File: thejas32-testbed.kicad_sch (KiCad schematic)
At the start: 101 parts, among them J1 Conn_01x04, J10 Conn_02x10_Odd_Even, J11 Conn_01x03, J12 Conn_02x20_Odd_Even, J13 Conn_01x03, J2 USB_B_Micro, J3 Conn_02x03_Odd_Even, J4 Conn_02x05_Odd_Even, J6 Conn_01x10, J7 Conn_01x05, J8 Conn_01x03, J9 Conn_01x05, U1 Pico Master, U2 THEJAS32, U6 W25Q16JVSSIQ

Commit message: Incorporated most review comments.
Used 5 mils traces in breakout area. This results in very few DRC
errors iff track spacing is set to 5 mils.  However, setting it to
8 mils (in board settings) does complain essentially for every pad
of the THEJAS32. Those just need to be waived off.

Ensure 16 mils track separation, except in breakout area. This can
be verified by setting the track spacing to 16 mils and running the
DRC. Except for the core area, and some issues on the USB connector,
no other errors must pop up.

Poured copper on every layer. Added GND vias to increase GND pour.

Moved flash IC to improve routing to the GPIO connector.

Moved USB connector close to the RP2040s USB connector, J3 placed
next to it. So both jumpers are now close.

Added MPN field, and populated it for many components, except caps
and headers.

Pending: Power nets are routed at 12 mils from THEJAS32. Get it down
to 5 mil ?
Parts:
- removed H5: MountingHole, MountingHole:MountingHole_3mm, symbol Mechanical:MountingHole
- R1, R16, R18, R20, R22, R24, R25, R26, R28, R29, R30, R31, R32, R33, R34, R35, R36, R37, R70: value 0E -> 27E; MPN (none) -> 27E
- R2, R38, R39, R40, R41, R42, R43: MPN (none) -> 10K
- R4, R5, R6, R7, R8, R9: MPN (none) -> 2.2K
- TP1: footprint MountingHole:MountingHole_3mm_Pad_TopBottom -> MountingHole:MountingHole_3.2mm_M3_Pad_TopBottom
- U1: MPN (none) -> Raspberry Pi Pico
- U2: MPN (none) -> THEJAS32
- U4, U5: MPN (none) -> Mini360
- U6: MPN (none) -> W25Q16JVSSIQ
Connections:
- net GND: now also J10.1 (Pin_1), J10.2 (Pin_2); no longer J10.19 (Pin_19), J10.20 (Pin_20)
- net PWR_3V3: now also J10.19 (Pin_19), J10.20 (Pin_20); no longer J10.1 (Pin_1), J10.2 (Pin_2)
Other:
- note added: "Jumper Meaning ------------------------------------------------------------- JP3 JP4 | ------------------------------------------------------------- Y Y | 5V from USB connector is used for the entire board. | Pico must not get power from host. | Pico can be used as USB host. ------------------------------------------------------------- N Y | 5V from USB connector is used for Thejas32 only. | Pico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"
- note added: "Power for THEJAS32"
- note added: "THEJAS32 Core Circuit"
- moved on the sheet: C1, C10, C10A1, C11, C11A1, C12, C12A1, C13, C14, C15, C16, C17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

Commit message: Cleanup and beautification for review.
Added silkscreen for all components.
Grouped schematic for reading clarity.
No circuit level changes, few nets renamed.
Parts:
- R1, R70: value 27E -> 10E; MPN 27E -> 10E
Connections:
- net MCU_BOOT_UART_RX: now also J3.3 (Pin_3), U2.107 (UART0_RX); no longer J3.4 (Pin_4), U1.6 (GPIO4)
- net MCU_BOOT_UART_TX: now also J3.1 (Pin_1), U2.108 (UART0_TX); no longer J3.2 (Pin_2), U1.7 (GPIO5)
- net MCU_UART1_TX: now reaches J11.1 (Pin_1), U2.45 (UART1_TX)
- net MCU_UART1_RX: now reaches J11.2 (Pin_2), U2.50 (UART1_RX)
- new net MCU_BOOT_UART_RX_PICO: J3.4 (Pin_4), U1.6 (GPIO4)
- new net MCU_BOOT_UART_TX_PICO: J3.2 (Pin_2), U1.7 (GPIO5)
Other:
- note added: "10K to ground, following official docs"
- note added: "Boot UART Tapping Header"
- note added: "GPOUT clock serves as the clock for THEJAS32. Nominal clock 100 MHz"
- note added: "Headers to tap I2C and SPI comms between THEJAS32 and Pico"
- note added: "JTAG connections"
- note added: "Jumper Usage"
- note added: "Pull-ups used as THEJAS32 doesn't have internal ones. Depop if not required."
- note added: "Raspberry Pi HAT Compatibility"
- note added: "Test Driver (Raspberry Pico)"
- note added: "This header is to help plug common hats and get them to work. From a pinmux and functionality perspective, thejas32 doesn't match the RPi, but this provides useful compatibility for commonly used pins. Thejas pins don't have pinmuxing. E.g. UART pins can't be used as GPIOs... The following are ensured: 3.3V, 5V for appropriately powering the HATs I2C on pins 3,5 UART RX, TX on pins 8, 10 SPI with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"
- note added: "User Headers"
- note removed: "GPOUT clock serves as the clock for THEJAS32"
- note removed: "Raspberry Pi Compatibility Header This header is to help plug common hats and get them to work. From a pinmux and functionality perspective, thejas32 doesn't match the RPi so it's a no-brainer that you should expect only some useful compatibility. Bear in mind that thejas pins have single functionality. E.g. UART pins can't be used as GPIOs... The following are ensured: 3.3V, 5V for appropriately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"
- moved on the sheet: H1, H2, H3, H4, J1, J10, J12, J13, J2, J3, J4, J6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

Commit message: Ready for review, all comments included
All MPNs are provided
Silkscreen updated
BOM generation corrected.
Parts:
- C1, C10, C11, C12, C13, C14, C15, C16, C17, C18, C19, C2, C20, C21, C22, C23, C24, C25, C3, C4, C5, C6, C7, C8, C9: MPN (none) -> 100nF
- C10A1, C11A1, C12A1, C1A1, C25A1, C2A1, C3A1, C4A1, C5A1, C6A1, C7A1, C8A1, C9A1: MPN (none) -> 10uF
- H1, H2, H3, H4, TP1, TP2, TP4, TP6, TP7: now left out of the parts list
- J1: MPN (none) -> 2.54 mm 1x4 pin male header
- J10: MPN (none) -> 2.54 mm 2x10 pin male header
- J11, J13, J8: MPN (none) -> 2.54 mm 1x3 pin male header
- J12: MPN (none) -> 2.54 mm 2x20 pin male header
- J3: MPN (none) -> 2.54 mm 2x3 pin male header
- J4: MPN (none) -> 2.54 mm 2x5 pin male header
- J6: MPN (none) -> 2.54 mm 1x10 pin male header
- J7, J9: MPN (none) -> 2.54 mm 1x5 pin male header
- JP1, JP2, JP3, JP4: MPN (none) -> 2.54 mm 1x2 pin male header
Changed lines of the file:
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@@
 			)
 		)
-		(property "MPN" ""
+		(property "MPN" "100nF"
 			(at 27.94 162.56 0)
 			(effects
@@
 			)
 		)
-		(property "MPN" ""
+		(property "MPN" "2.54 mm 1x5 pin male header"
 			(at 472.44 492.76 0)
 			(effects
@@
 			)
 		)
-		(property "MPN" ""
+		(property "MPN" "100nF"
 			(at 54.61 219.71 0)
 			(effects
@@
 			)
 		)
-		(property "MPN" ""
+		(property "MPN" "2.54 mm 1x10 pin male header"
 			(at 542.29 335.28 0)
 			(effects
@@
 			)
 		)
-		(property "MPN" ""
+		(property "MPN" "100nF"
 			(at 81.28 290.83 0)
 			(effects
@@
 			)
 		)
-		(property "MPN" ""
+		(property "MPN" "2.54 mm 1x3 pin male header"
 			(at 275.59 316.23 0)
 			(effects
@@
 			)
 		)
-		(property "MPN" ""
+		(property "MPN" "10uF"
 			(at 39.37 167.64 0)
 			(effects
@@
 			)
 		)
-		(property "MPN" ""
+		(property "MPN" "2.54 mm 1x5 pin male header"
 			(at 294.64 551.18 0)
 			(effects
@@
 			)
 		)
-		(property "MPN" ""
+		(property "MPN" "100nF"
 			(at 101.6 243.84 0)
 			(effects
@@
 			)
 		)
-		(property "MPN" ""
+		(property "MPN" "100nF"
 			(at 92.71 243.84 0)
 			(effects
@@
 		(unit 1)
 		(exclude_from_sim no)
-		(in_bom yes)
+		(in_bom no)
 		(on_board yes)
 		(dnp no)
@@
 			)
 		)
-		(property "MPN" ""
+		(property "MPN" "100nF"
 			(at 92.71 265.43 0)
 			(effects
@@
 			)
 		)
-		(property "MPN" ""
+		(property "MPN" "100nF"
 			(at 82.55 243.84 0)
 			(effects
@@
 			)
 		)
-		(property "MPN" ""
+		(property "MPN" "100nF"
 			(at 80.01 123.19 0)
 			(effects
@@
 			)
 		)
-		(property "MPN" ""
+		(property "MPN" "100nF"
 			(at 100.33 290.83 0)
 			(effects
@@
 		(unit 1)
 		(exclude_from_sim no)
-		(in_bom yes)
+		(in_bom no)
 		(on_board yes)
 		(dnp no)
@@
 			)
 		)
-		(property "MPN" ""
+		(property "MPN" "100nF"
 			(at 101.6 265.43 0)
 			(effects
@@
 			)
 		)
-		(property "MPN" ""
+		(property "MPN" "100nF"
 			(at 93.98 219.71 0)
 			(effects
@@
 			)
 		)
-		(property "MPN" ""
+		(property "MPN" "100nF"
 			(at 370.84 295.91 0)
 			(effects
@@
 			)
 		)
-		(property "MPN" ""
+		(property "MPN" "2.54 mm 1x2 pin male header"
 			(at 576.58 213.36 0)
 			(effects
@@
 		(unit 1)
 		(exclude_from_sim no)
-		(in_bom yes)
+		(in_bom no)
 		(on_board yes)
 		(dnp no)
@@
 			)
 		)
-		(property "MPN" ""
+		(property "MPN" "2.54 mm 2x5 pin male header"
 			(at 378.46 547.37 0)
 			(effects
@@
 			)
 		)
-		(property "MPN" ""
+		(property "MPN" "2.54 mm 1x4 pin male header"
 			(at 643.89 313.69 0)
 			(effects
@@
 			)
 		)
-		(property "MPN" ""
+		(property "MPN" "100nF"
 			(at 327.66 132.08 0)
 			(effects
@@
 		(unit 1)
 		(exclude_from_sim no)
-		(in_bom yes)
+		(in_bom no)
 		(on_board yes)
 		(dnp no)
@@
 			)
 		)
-		(property "MPN" ""
+		(property "MPN" "2.54 mm 1x3 pin male header"
 			(at 566.42 303.53 0)
 			(effects
@@
 			)
 		)
-		(property "MPN" ""
+		(property "MPN" "100nF"
 			(at 82.55 265.43 0)
 			(effects
@@
 		(unit 1)
 		(exclude_from_sim no)
-		(in_bom yes)
+		(in_bom no)
 		(on_board yes)
 		(dnp no)
@@
 			)
 		)
-		(property "MPN" ""
+		(property "MPN" "10uF"
 			(at 383.54 274.32 0)
 			(effects
@@
 			)
 		)
-		(property "MPN" ""
+		(property "MPN" "100nF"
 			(at 288.29 132.08 0)
 			(effects
@@
 		(unit 1)
 		(exclude_from_sim no)
-		(in_bom yes)
+		(in_bom no)
 		(on_board yes)
 		(dnp no)
@@
 			)
 		)
-		(property "MPN" ""
+		(property "MPN" "10uF"
 			(at 64.77 219.71 0)
 			(effects
@@
 			)
 		)
-		(property "MPN" ""
+		(property "MPN" "2.54 mm 1x2 pin male header"
 			(at 627.38 297.18 0)
 			(effects
@@
 			)
 		)
-		(property "MPN" ""
+		(property "MPN" "10uF"
 			(at 344.17 274.32 0)
 			(effects
@@
 			)
 		)
-		(property "MPN" ""
+		(property "MPN" "2.54 mm 1x3 pin male header"
 			(at 514.35 490.22 0)
 			(effects
@@
 			)
 		)
-		(property "MPN" ""
+		(property "MPN" "100nF"
 			(at 71.12 123.19 0)
 			(effects
@@
 			)
 		)
-		(property "MPN" ""
+		(property "MPN" "10uF"
 			(at 298.45 132.08 0)
 			(effects
@@
 		(unit 1)
 		(exclude_from_sim no)
-		(in_bom yes)
+		(in_bom no)
 		(on_board yes)
 		(dnp no)
@@
 			)
 		)
-		(property "MPN" ""
+		(property "MPN" "100nF"
 			(at 60.96 123.19 0)
 			(effects
@@
 		(unit 1)
 		(exclude_from_sim no)
-		(in_bom yes)
+		(in_bom no)
 		(on_board yes)
 		(dnp no)
@@
 			)
 		)
-		(property "MPN" ""
+		(property "MPN" "10uF"
 			(at 83.82 219.71 0)
 			(effects
@@
 			)
 		)
-		(property "MPN" ""
+		(property "MPN" "10uF"
 			(at 317.5 133.35 0)
 			(effects
@@
 			)
 		)
-		(property "MPN" ""
+		(property "MPN" "100nF"
 			(at 120.65 290.83 0)
 			(effects
@@
 		(unit 1)
 		(exclude_from_sim no)
-		(in_bom yes)
+		(in_bom no)
 		(on_board yes)
 		(dnp no)
@@
 			)
 		)
-		(property "MPN" ""
+		(property "MPN" "10uF"
 			(at 110.49 290.83 0)
 			(effects
@@
 			)
 		)
-		(property "MPN" ""
+		(property "MPN" "2.54 mm 2x10 pin male header"
 			(at 382.27 500.38 0)
 			(effects
@@
 			)
 		)
-		(property "MPN" ""
+		(property "MPN" "100nF"
 			(at 334.01 274.32 0)
 			(effects
@@
 			)
 		)
-		(property "MPN" ""
+		(property "MPN" "100nF"
 			(at 373.38 274.32 0)
 			(effects
@@
 			)
 		)
-		(property "MPN" ""
+		(property "MPN" "100nF"
 			(at 73.66 219.71 0)
 			(effects
@@
 			)
 		)
-		(property "MPN" ""
+		(property "MPN" "100nF"
 			(at 307.34 132.08 0)
 			(effects
@@
 			)
 		)
-		(property "MPN" ""
+		(property "MPN" "2.54 mm 1x2 pin male header"
 			(at 575.31 180.34 0)
 			(effects
@@
 			)
 		)
-		(property "MPN" ""
+		(property "MPN" "2.54 mm 1x2 pin male header"
 			(at 516.89 172.72 0)
 			(effects
@@
 			)
 		)
-		(property "MPN" ""
+		(property "MPN" "10uF"
 			(at 363.22 274.32 0)
 			(effects
@@
 			)
 		)
-		(property "MPN" ""
+		(property "MPN" "10uF"
 			(at 104.14 219.71 0)
 			(effects
@@
 			)
 		)
-		(property "MPN" ""
+		(property "MPN" "100nF"
 			(at 379.73 295.91 0)
 			(effects
@@
 			)
 		)
-		(property "MPN" ""
+		(property "MPN" "2.54 mm 2x3 pin male header"
 			(at 281.94 487.68 0)
 			(effects
@@
 			)
 		)
-		(property "MPN" ""
+		(property "MPN" "100nF"
 			(at 353.06 274.32 0)
 			(effects
@@
 			)
 		)
-		(property "MPN" ""
+		(property "MPN" "10uF"
 			(at 337.82 132.08 0)
 			(effects
@@
 			)
 		)
-		(property "MPN" ""
+		(property "MPN" "100nF"
 			(at 360.68 295.91 0)
 			(effects
@@
 			)
 		)
-		(property "MPN" ""
+		(property "MPN" "10uF"
 			(at 91.44 290.83 0)
 			(effects
@@
 			)
 		)
-		(property "MPN" ""
+		(property "MPN" "2.54 mm 2x20 pin male header"
 			(at 100.33 519.43 0)
 			(effects
@@
 			)
 		)
-		(property "MPN" ""
+		(property "MPN" "10uF"
 			(at 130.81 290.83 0)
 			(effects

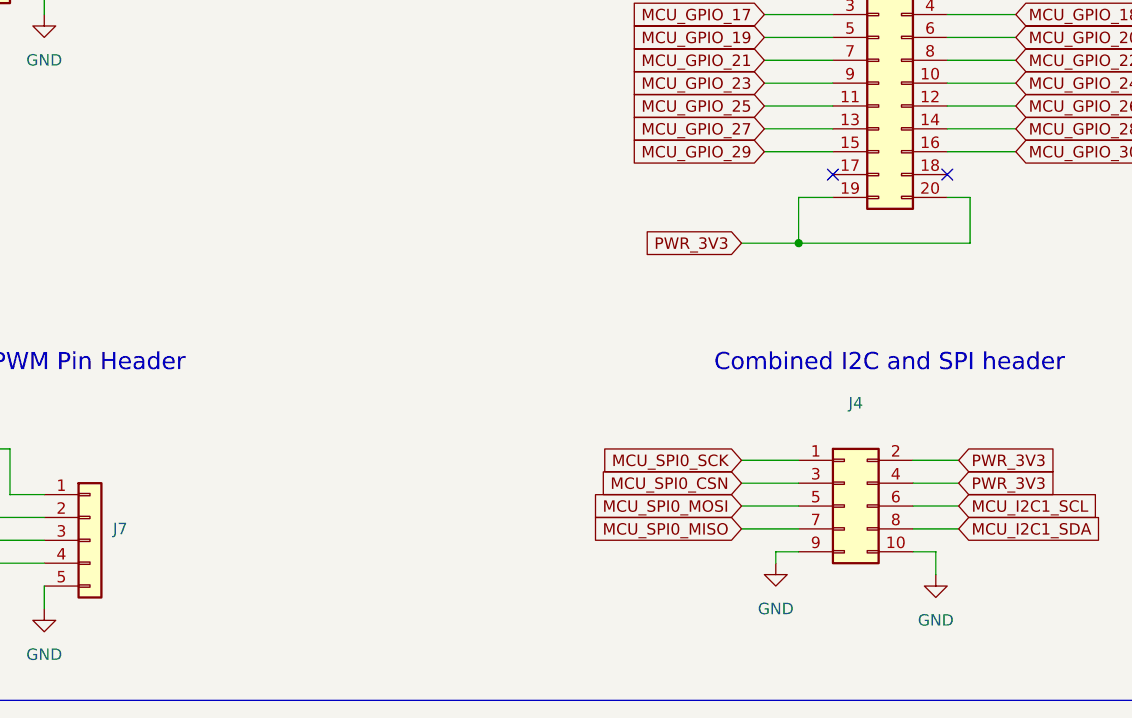
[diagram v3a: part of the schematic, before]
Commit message: Updates from review
Some major changes:
1. JTAG connector
2. Cleaned up layout in breakout area
3. Improved MCU_CLOCK routing
4. Alignment on right side jumpers
5. 5V included in J10
6. Ground guarding vias around edge

Ref: review of July 20

Updates the silkscreen as well
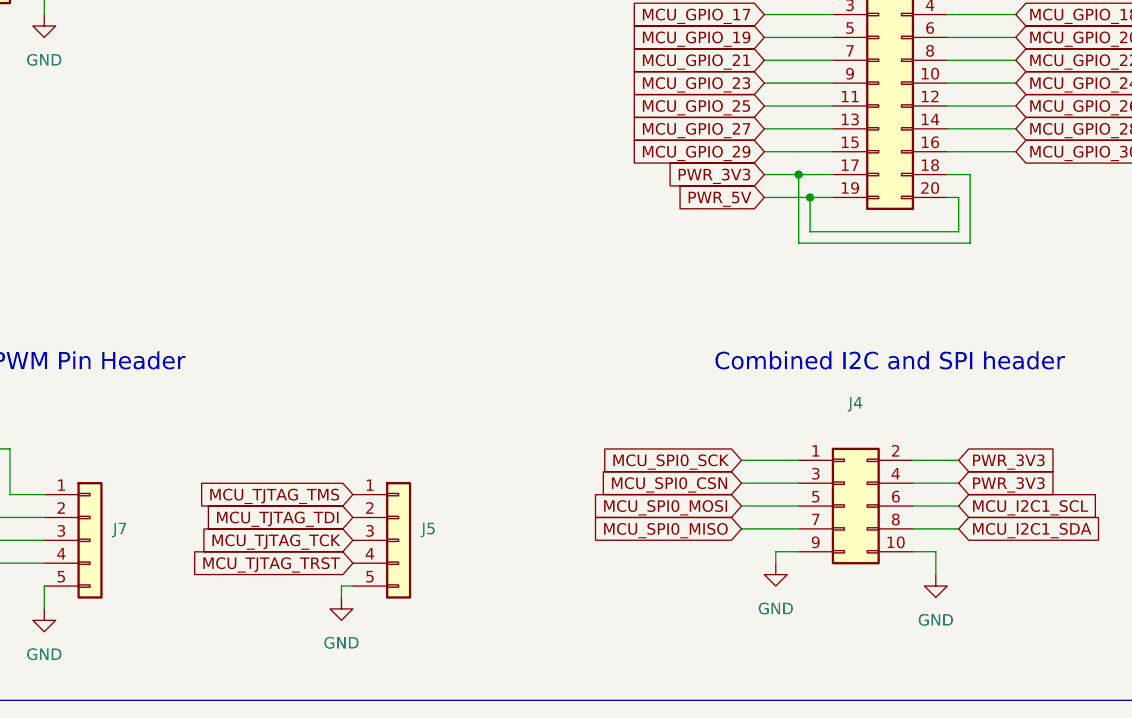
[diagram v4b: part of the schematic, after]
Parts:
- added J5: Conn_01x05, Connector_PinHeader_2.54mm:PinHeader_1x05_P2.54mm_Vertical, symbol Connector_Generic:Conn_01x05
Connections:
- net GND: now also J5.5 (Pin_5)
- net MCU_TJTAG_TCK: now also J5.3 (Pin_3)
- net MCU_TJTAG_TDI: now also J5.2 (Pin_2)
- net MCU_TJTAG_TMS: now also J5.1 (Pin_1)
- net MCU_TJTAG_TRST: now also J5.4 (Pin_4)
- net PWR_3V3: now also J10.17 (Pin_17), J10.18 (Pin_18); no longer J10.19 (Pin_19), J10.20 (Pin_20)
- net PWR_5V: now also J10.19 (Pin_19), J10.20 (Pin_20)
- no-connect marks 16 -> 14

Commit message: Doc updates
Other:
- note removed: "Aligned Mounting holes"
- note removed: "Change R2 to 100k for weak PD"
- note removed: "Change R3 to 100k for weak PD"
- note removed: "DEbug UART 0 for master Pico is not conneted anywhere"
- note removed: "Need to add Properties like MPN Manufacturer in properties for easier BOM creation"
- note removed: "Need to check of R4/R5 has any PU for I2C on Main RasPi. If there, remove R4/R5"
- title: (none) -> THEJAS32 Testbed
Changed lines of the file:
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@@
 	(generator_version "8.0")
 	(paper "A1")
+	(title_block
+		(title "THEJAS32 Testbed")
+	)
 	(junction
 		(at 373.38 510.54)
@@
 		)
 	)
-	(text "Aligned Mounting holes"
-		(exclude_from_sim no)
-		(at 744.474 64.516 0)
-		(effects
-			(font
-				(size 1.27 1.27)
-				(color 255 30 34 1)
-			)
-			(justify left bottom)
-		)
-	)
 	(text "MCU_BOOT_UART can be used to program\nMCU using ZMODEM. Also boot messages,\nprintf, etc. This is uart1 of RP2040"
 		(exclude_from_sim no)
@@
 		)
 	)
-	(text "Need to check of R4/R5 has any PU for I2C on Main RasPi. \nIf there, remove R4/R5"
-		(exclude_from_sim no)
-		(at 744.982 36.322 0)
-		(effects
-			(font
-				(size 1.27 1.27)
-				(color 255 30 34 1)
-			)
-			(justify left bottom)
-		)
-	)
 	(text "THEJAS32 Core Circuit"
 		(exclude_from_sim no)
@@
 		)
 	)
-	(text "When Powering through RasPi, remove JP1"
-		(exclude_from_sim no)
-		(at 744.982 44.958 0)
-		(effects
-			(font
-				(size 1.27 1.27)
-				(color 255 30 34 1)
-			)
-			(justify left bottom)
-		)
-	)
 	(text "The flash circuit is from the Raspberry\nPi Pico design. Larger dcap is 1005 in \nthat  design, with value 2.2uF"
 		(exclude_from_sim no)
@@
 		)
 	)
-	(text "Change R2 to 100k for weak PD\n"
-		(exclude_from_sim no)
-		(at 744.728 26.924 0)
-		(effects
-			(font
-				(size 1.27 1.27)
-				(color 255 30 34 1)
-			)
-			(justify left bottom)
-		)
-	)
 	(text "Jumper     Meaning\n-------------------------------------------------------------\nJP3 JP4 |\n-------------------------------------------------------------\nY   Y   | 5V from USB connector is used for the entire board.\n        | Pico must not get power from host.\n        | Pico can be used as USB host.\n-------------------------------------------------------------\nN   Y   | 5V from USB connector is used for Thejas32 only.\n        | Pico must be powered using its USB connector.\n-------------------------------------------------------------\nY   N   | Single cable mode. USB connector is not used\n        | Pico must be powered using its USB connector\n        | This power is used to run Thejas32 also\n-------------------------------------------------------------"
 		(exclude_from_sim no)
@@
 		)
 	)
-	(text "Need to add Properties like\nMPN\nManufacturer \nin properties for easier BOM creation"
-		(exclude_from_sim no)
-		(at 744.982 22.352 0)
-		(effects
-			(font
-				(size 1.27 1.27)
-				(color 255 30 34 1)
-			)
-			(justify left bottom)
-		)
-	)
 	(text "See layout instructions for decaps"
 		(exclude_from_sim no)
@@
 		)
 	)
-	(text "DEbug UART 0 for master Pico is not conneted anywhere"
-		(exclude_from_sim no)
-		(at 744.982 41.148 0)
-		(effects
-			(font
-				(size 1.27 1.27)
-				(color 255 30 34 1)
-			)
-			(justify left bottom)
-		)
-	)
 	(text "See layout instructions for decaps"
 		(exclude_from_sim no)
@@
 		)
 	)
-	(text "Change R3 to 100k for weak PD\n"
-		(exclude_from_sim no)
-		(at 744.982 30.734 0)
-		(effects
-			(font
-				(size 1.27 1.27)
-				(color 255 30 34 1)
-			)
-			(justify left bottom)
-		)
-	)

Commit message: USB footprint changed to Molex-105017-0001
This component is very close to Sunrom Part 4653

https://www.sunrom.com/p/microusb-connector-with-through-hole-support-legs

I am using the footprint from Molex, but the board
will use the Sunrom part.
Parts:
- J2: footprint Connector_USB:USB_Micro-B_Wuerth_629105150521_CircularHoles -> Connector_USB:USB_Micro-B_Molex-105017-0001
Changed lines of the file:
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@@
 			)
 		)
-		(property "Footprint" "Connector_USB:USB_Micro-B_Wuerth_629105150521_CircularHoles"
+		(property "Footprint" "Connector_USB:USB_Micro-B_Molex-105017-0001"
 			(at 505.46 179.07 0)
 			(effects

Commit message: Fix component properties
Added manufacturer, corrected MPN and description
These aren't provided for berg connectors
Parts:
- C1, C10, C11, C12, C13, C14, C15, C16, C17, C18, C19, C2, C20, C21, C22, C23, C24, C25, C3, C4, C5, C6, C7, C8, C9: MPN 100nF -> 5190; Manufacturer (none) -> Sunrom
- C10A1, C11A1, C12A1, C1A1, C25A1, C2A1, C3A1, C4A1, C5A1, C6A1, C7A1, C8A1, C9A1: MPN 10uF -> 6799; Manufacturer (none) -> Sunrom
- J2: MPN (none) -> 4653; Manufacturer (none) -> Sunrom
- R1, R70: MPN 10E -> 5354; Manufacturer (none) -> Sunrom
- R16, R18, R20, R22, R24, R25, R26, R28, R29, R30, R31, R32, R33, R34, R35, R36, R37: MPN 27E -> 5297; Manufacturer (none) -> Sunrom
- R2, R38, R39, R40, R41, R42, R43: MPN 10K -> 5192; Manufacturer (none) -> Sunrom
- R4, R5, R6, R7, R8, R9: MPN 2.2K -> 6735; Manufacturer (none) -> Sunrom
- U1: Manufacturer (none) -> Raspberry Pi
- U2: Manufacturer (none) -> CDAC
- U4, U5: MPN Mini360 -> 790469; Manufacturer (none) -> Robu
- U6: Manufacturer (none) -> Winbond
